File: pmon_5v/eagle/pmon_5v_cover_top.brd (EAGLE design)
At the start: 66 x 66 mm, 4 parts, among them J1 USB, J2 USB

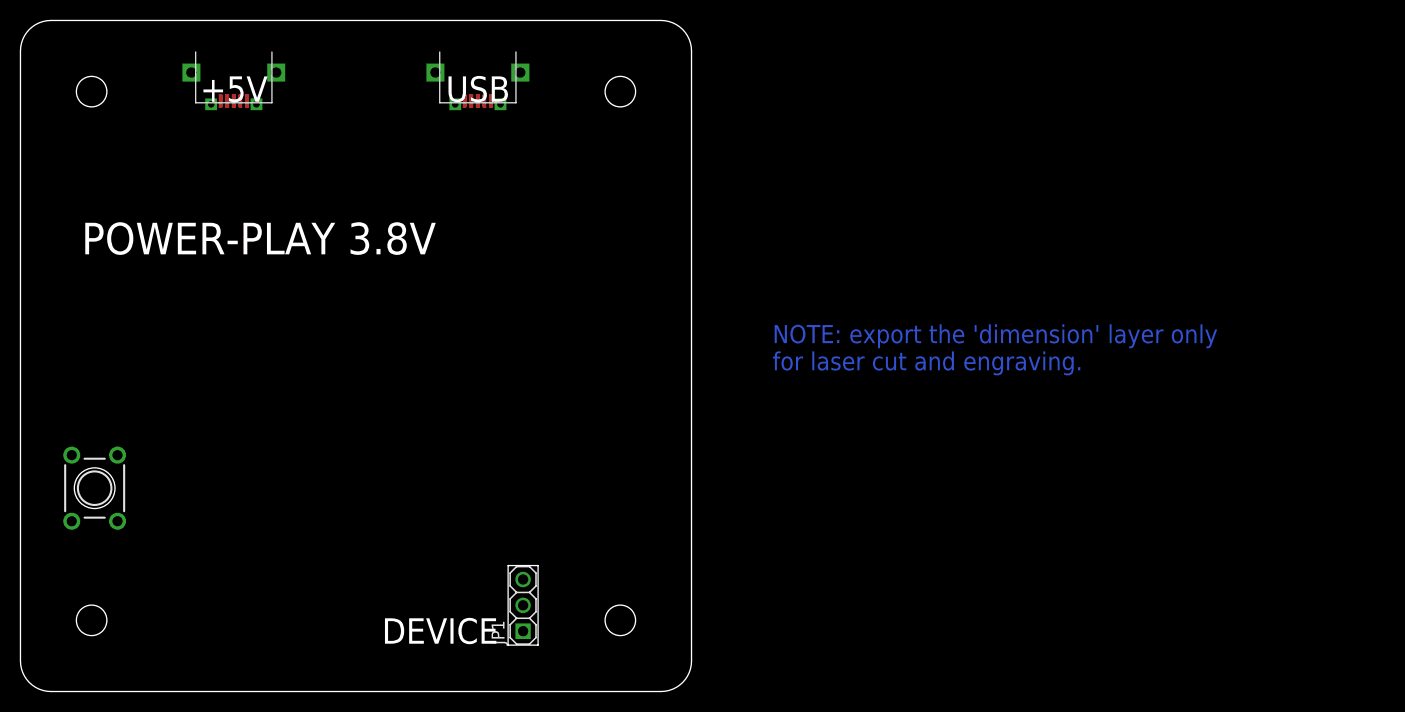
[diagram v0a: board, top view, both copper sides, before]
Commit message: Cleaned up laser cut files.
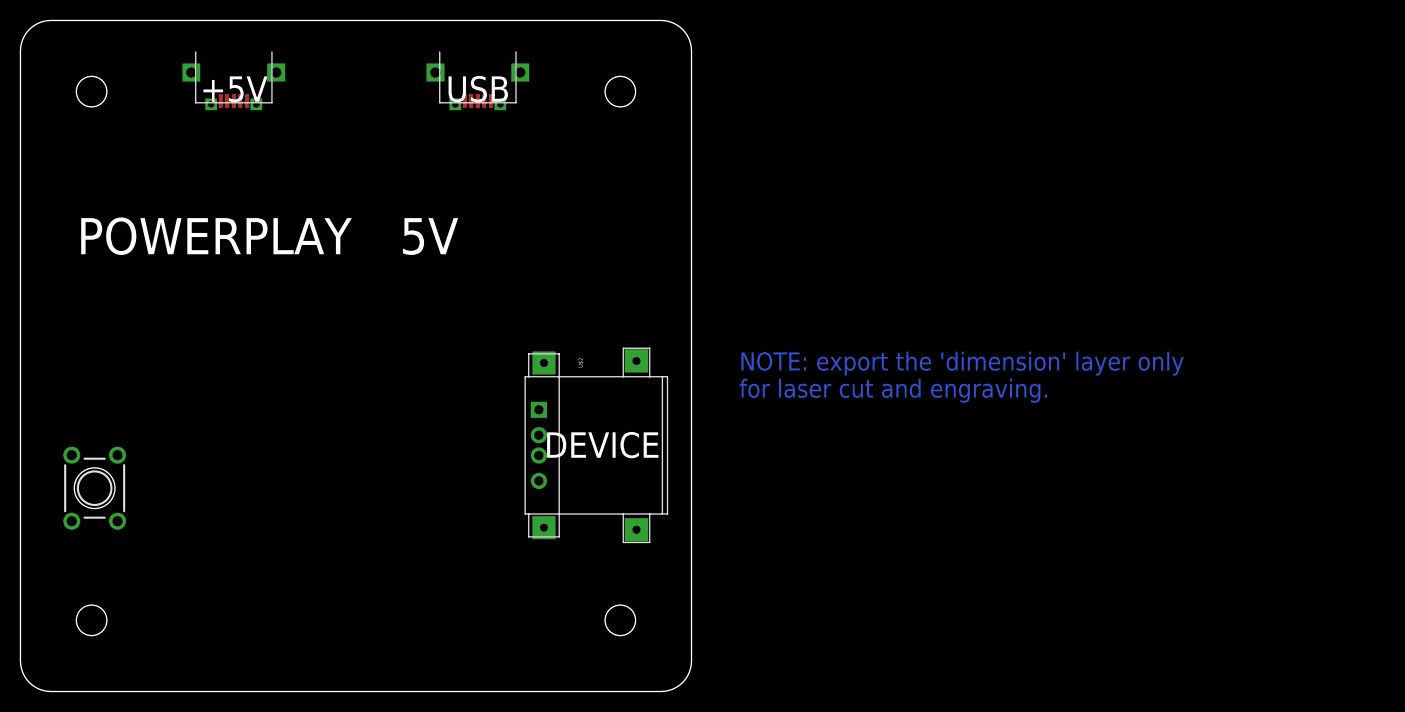
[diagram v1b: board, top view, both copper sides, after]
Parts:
- removed JP1: (no value), pmon_oled:1X03
- added U$2: USB_A, pmon_5v:USB_A
- J1, J2: device pmon_3v8:USB-MICRO-ZX62RD-AB-5P8 -> pmon_5v:USB-MICRO-ZX62RD-AB-5P8
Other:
- outline, holes or cut-outs redrawn
- board text added: "5V"
- board text added: "POWERPLAY"
- board text removed: "POWER-PLAY 3.8V"
